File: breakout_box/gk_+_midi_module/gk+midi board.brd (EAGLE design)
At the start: 65.2 x 100 mm, 114 parts, among them Q1 QUARZ5, T1 2N2222, T2 2N2222, U1 LMV324, U3 L78LXX, U4 MIC5205-3.3, U5 MSP430G2553RHB32, U7 TLV2170DGKT

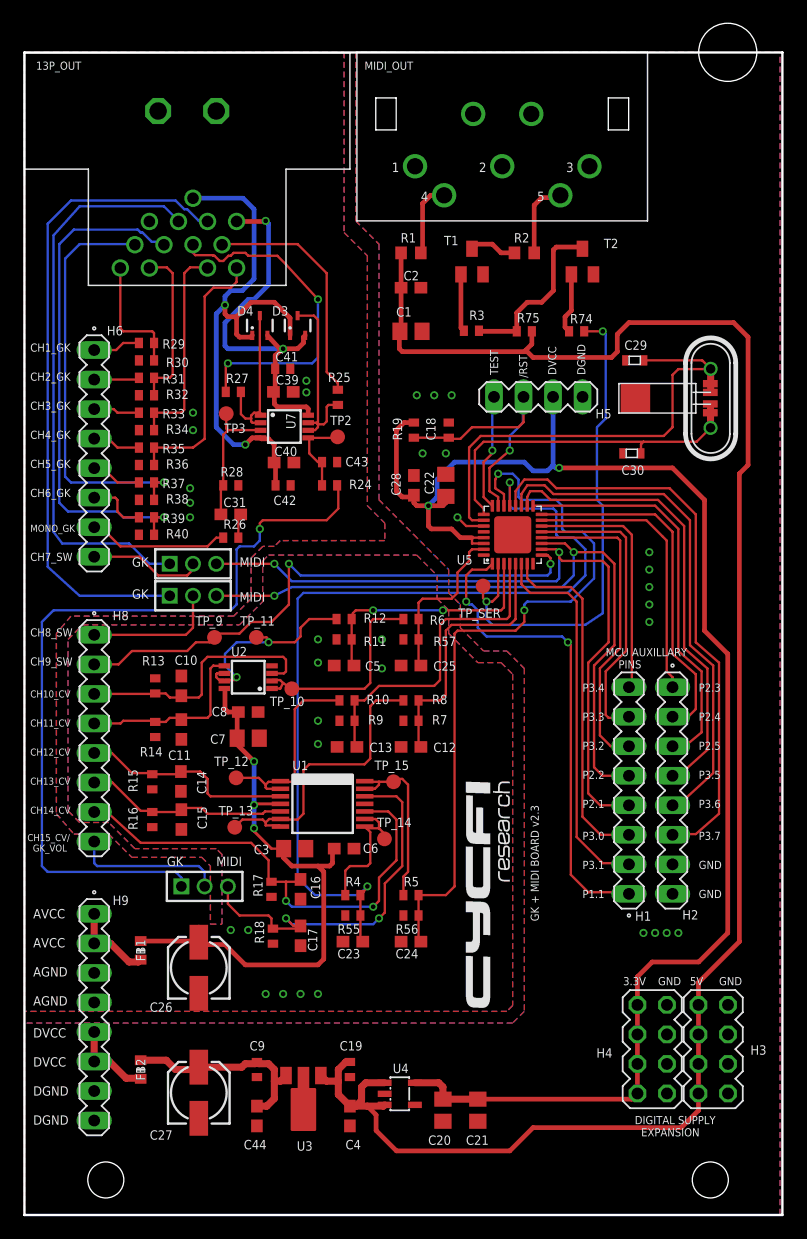
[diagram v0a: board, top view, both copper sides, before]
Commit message: update boms and pdf for shematics files
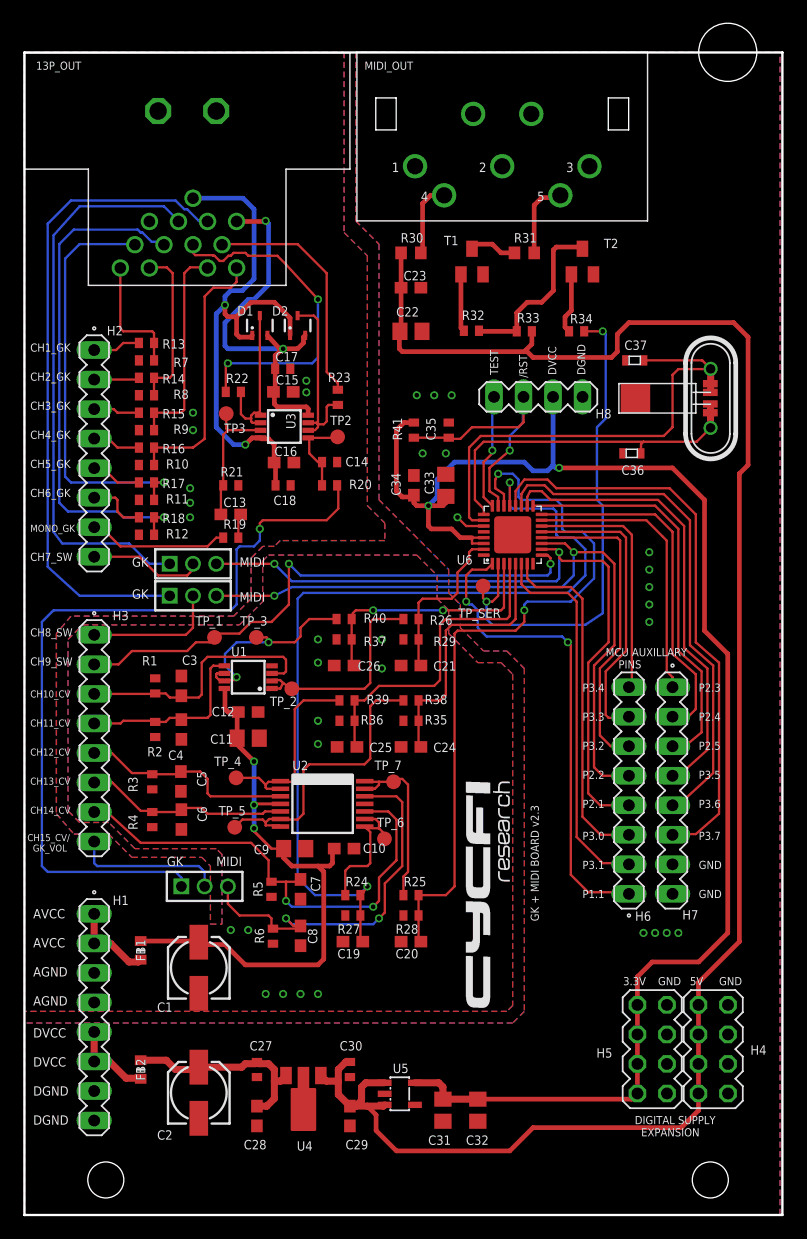
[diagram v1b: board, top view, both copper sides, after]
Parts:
- removed C39, C40: 4.7uF, resistor:C0603
- removed C41, C42: 0.1uF, resistor:C0402
- removed C43: 0.01uF, resistor:C0402
- removed C44: 0.1uF, resistor:C0603
- removed H9: (no value), con-lstb:MA08-1
- removed R55, R56, R57: 10k, resistor:R0402
- removed R74, R75: 1K, resistor:R0402
- removed U7: TLV2170DGKT, CYCFI_semicon:MSOP8
- added C32: 10uf, resistor:C0805
- added C33: 2.2uf, resistor:C0805
- added C34: 0.1uf, resistor:C0603
- added C35: 1nF, resistor:C0402
- added C36, C37: 12pF, ssmd:0603
- added H7: DNP, con-lstb:MA08-1
- added R20: 18K, resistor:R0402
- added R21: 470K, resistor:R0402
- added R22, R23: 100R, resistor:R0402
- added R41: 47K, resistor:R0402
- added U6: MSP430G2553RHB32, CYCFI_IC:QFN32
- C1: value 10uF -> 100uF; device resistor:C0805 -> resistor:153CLV-0505
- C11: value 0.1uF -> 10uF; device resistor:C0603 -> resistor:C0805
- C13: value 0.1uF -> 0.47uF
- C14: value 0.1uF -> 0.01uF; device resistor:C0603 -> resistor:C0402
- C15, C16: value 0.1uF -> 4.7uF
- C17: device resistor:C0603 -> resistor:C0402
- C18: value 1nF -> 0.1uF
- C19: value 1uF -> 0.1uF; device resistor:C0402 -> resistor:C0603
- C2: value 0.1uF -> 100uF; device resistor:C0603 -> resistor:153CLV-0505
- C20: value 33uf -> 0.1uF; device resistor:C0805 -> resistor:C0603
- C21: value 10uf -> 0.1uF; device resistor:C0805 -> resistor:C0603
- C22: value 2.2uf -> 10uF
- C26: value 100uF -> 0.1uF; device resistor:153CLV-0505 -> resistor:C0603
- C27: value 100uF -> 1uF; device resistor:153CLV-0505 -> resistor:C0402
- C28: value 0.1uf -> 0.1uF
- C29: value 12pF -> 0.1uF; device ssmd:0603 -> resistor:C0603
- C3, C7: value 10uF -> 0.1uF; device resistor:C0805 -> resistor:C0603
- C30: value 12pF -> 1uF; device ssmd:0603 -> resistor:C0402
- C31: value 0.47uF -> 33uf; device resistor:C0603 -> resistor:C0805
- C9: value 1uF -> 10uF; device resistor:C0402 -> resistor:C0805
- H1, H2: value DNP -> (none)
- H3: value DNP -> (none); device con-lstb:MA04-2 -> con-lstb:MA08-1
- H5: value (none) -> DNP; device con-lstb:MA04-1 -> con-lstb:MA04-2
- H6: value (none) -> DNP
- H8: device con-lstb:MA08-1 -> con-lstb:MA04-1
- R1, R2: value 220R -> 100K; device resistor:R0603 -> resistor:R0402
- R10, R12, R8: value 5.1k -> 5k
- R11, R7, R9: value 10k -> 5k
- R13, R14, R15, R16, R17, R18: value 100K -> 5k
- R19: value 47K -> 10K
- R24: value 18K -> 5.1k
- R25: value 100R -> 5.1k
- R26: value 10K -> 5.1k
- R27: value 100R -> 10k
- R28: value 470K -> 10k
- R29, R35, R36, R37: value 5k -> 10k
- R3: value 1K -> 100K
- R30, R31: value 5k -> 220R; device resistor:R0402 -> resistor:R0603
- R32, R33, R34: value 5k -> 1K
- R38, R39, R40: value 5k -> 5.1k
- R4, R5, R6: value 5.1k -> 100K
- U1: value LMV324 -> (none); device CYCFI_semicon:SSOP-14 -> CYCFI_semicon:MSOP8
- U2: value (none) -> LMV324; device CYCFI_semicon:MSOP8 -> CYCFI_semicon:SSOP-14
- U3: value L78LXX -> TLV2170DGKT; device CYCFI_Power:SOT89 -> CYCFI_semicon:MSOP8
- U4: value MIC5205-3.3 -> L78LXX; device v-reg-micrel:SOT23-5 -> CYCFI_Power:SOT89
- U5: value MSP430G2553RHB32 -> MIC5205-3.3; device CYCFI_IC:QFN32 -> v-reg-micrel:SOT23-5
- moved C2 71.6 mm to (15.0, 10.5), turned to 90 degrees
- moved C29 69.5 mm to (28.0, 8.50), turned to 270 degrees
- moved H3 59.6 mm to (6.00, 41.0), turned to 270 degrees
- moved C30 58.3 mm to (28.0, 12.5), turned to 270 degrees
- moved U3 57.8 mm to (22.4, 67.8), turned to 270 degrees
- moved C1 57.7 mm to (15.0, 21.2), turned to 90 degrees
- moved H2 57.6 mm to (6.00, 65.5)
- moved H5 57.0 mm to (54.0, 14.2), turned to 90 degrees
- moved C23 56.5 mm to (33.2, 79.8), turned to 0 degrees
- moved C28 55.9 mm to (20.0, 8.50), turned to 270 degrees
- moved C31 54.4 mm to (36.0, 9.00), turned to 270 degrees
- moved H6 54.4 mm to (52.0, 36.5), turned to 90 degrees
- moved R2 51.9 mm to (11.2, 41.8), turned to 90 degrees
- moved H1 50.0 mm to (6.00, 17.0), turned to 270 degrees
- moved U5 49.1 mm to (32.3, 10.4), turned to 270 degrees
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- renumbered D3 to D2, D4 to D1, TP_10 to TP_2, TP_11 to TP_3, TP_12 to TP_4, TP_13 to TP_5, TP_14 to TP_6, TP_15 to TP_7, TP_9 to TP_1, U$3 to U$1
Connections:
- net !RST: now also C35.1, H8.2, R41.2, U6.23; no longer C18.1, H5.2, R19.2, U5.23
- net +3.3V: now also C31.1, C32.1, C33.1, C34.1, H5.2, H5.4, H5.6, H5.8, H8.3, R41.1, U5.5, U6.29, U6.30; no longer C20.1, C21.1, C22.1, C28.1, H4.2, H4.4, H4.6, H4.8, H5.3, R19.1, U4.5, U5.29, U5.30
- net +5V: now also C22.1, C23.1, C29.1, C30.1, H4.2, H4.4, H4.6, H4.8, R30.1, R33.2, U5.1, U5.3; no longer C1.1, C19.1, C2.1, C4.1, H3.2, H3.4, H3.6, H3.8, R1.1, R75.2, U3.1, U4.3
- net +VE: now also C15.1, C17.1, U3.8; no longer C39.1, C41.1, U7.8
- net -VE: now also C16.2, C18.2, U3.4; no longer C40.2, C42.2, U7.4
- net AVCC: now also H1.1, H1.2; no longer H9.1, H9.2
- net CH10_CV: now also R26.1, U1.1, U1.2; no longer R6.1, U2.1, U2.2
- net CH11_CV: now also R40.2, U1.6, U1.7; no longer R12.2, U2.6, U2.7
- net CH12_CV: now also R39.2, U2.1, U2.2; no longer R10.2, U1.1, U1.2
- net CH13_CV: now also R38.2, U2.6, U2.7; no longer R8.2, U1.6, U1.7
- net CH14_CV: now also R24.1, U2.8, U2.9; no longer R4.1, U1.8, U1.9
- net CH15_CV: now also R25.1, U2.13, U2.14; no longer R5.1, U1.13, U1.14
- net CH15_CV_IN: now also C8.1, JP1.3, R6.2, U2.12; no longer C17.1, JP3.3, R18.2, U1.12
- net CH15_GK_VOL: now also JP1.1, R20.1; no longer JP3.1, R24.1
- net CH15_GK_VOL/CV: now also H3.8, JP1.2; no longer H8.8, JP3.2
- net CH1_GK: now also H2.1, R7.2; no longer H6.1, R30.2
- net CH2_GK: now also H2.2, R8.2; no longer H6.2, R32.2
- net CH3_GK: now also H2.3, R9.2; no longer H6.3, R34.2
- net CH4_GK: now also H2.4, R10.2; no longer H6.4, R36.2
- net CH5_GK: now also H2.5, R11.2; no longer H6.5, R38.2
- net CH6_GK: now also H2.6, R12.2; no longer H6.6, R40.2
- net CH7_CV_IN: now also H6.4, U6.10; no longer H1.4, U5.10
- net CH7_GK_SW/CV: now also H2.8; no longer H6.8
- net CH8_CV_IN: now also H6.5, JP3.3, U6.11; no longer H1.5, JP1.3, U5.11
- net CH8_GK_SW: now also JP3.1; no longer JP1.1
- net CH8_GK_SW/CV: now also H3.1, JP3.2; no longer H8.1, JP1.2
- net CH9_CV: now also H3.2, U6.9; no longer H8.2, U5.9
- net DVCC: now also H1.5, H1.6; no longer H9.5, H9.6
- net D_VIN: now also C2.+, C27.1, C28.1, U4.3; no longer C27.+, C44.1, C9.1, U3.3
- net GK_VOL: now also R23.2; no longer R25.2
- net GND: now also C1.-, C16.1, C18.1, C2.-, C26.2, C27.2, C29.2, C30.2, C31.2, C32.2, C33.2, C34.2, C35.2, C36.1, C37.1, H1.3, H1.4, H1.7, H1.8, H5.1, H5.3, H5.5, H5.7, H7.7, H7.8, H8.4, R1.1, R2.1, R21.2, R27.2, R29.2, R3.1, R35.2, R36.2, R37.2, R4.1, R5.1, R6.1, U1.4, U2.11, U4.2@1, U5.2, U6.27, U6.28; no longer C1.2, C13.2, C16.2, C18.2, C2.2, C26.-, C27.-, C29.1, C30.1, C39.2, C40.1, C41.2, C42.1, C43.2, C44.2, H2.7, H2.8, H3.1, H3.3, H3.5, H3.7, H5.4, H9.3, H9.4, H9.7, H9.8, R11.2, R29.1, R31.1, R33.1, R35.1, R37.1, R39.1, R55.2, R56.2, R57.2, R7.2, R9.2, U1.11, U2.4, U3.2, U3.2@1, U5.27, U5.28
- net MONO_GK: now also H2.7, R19.1; no longer H6.7, R26.1
- net N$1: now also R31.2; no longer R2.2
- net N$10: now also C3.1, H3.3, R1.2, U1.3; no longer C10.1, H8.3, R13.2, U2.3
- net N$11: now also C4.1, H3.4, R2.2, U1.5; no longer C11.1, H8.4, R14.2, U2.5
- net N$14: now also C5.1, H3.5, R3.2, U2.3; no longer C14.1, H8.5, R15.2, U1.3
- net N$19: now also C6.1, H3.6, R4.2, U2.5; no longer C15.1, H8.6, R16.2, U1.5
- net N$2: now also R31.1; no longer R2.1
- net N$20: now also C7.1, H3.7, R5.2, U2.10; no longer C16.1, H8.7, R17.2, U1.10
- net N$21: now also R22.1; no longer R27.1
- net N$3: now also R32.2; no longer R3.2
- net N$35: now also R23.1, U3.6, U3.7; no longer R25.1, U7.6, U7.7
- net N$36: now also C14.1, R20.2, U3.5; no longer C43.1, R24.2, U7.5
- net N$37: now also C13.2, R19.2; no longer C31.2, R26.2
- net N$38: now also C13.1, R21.1, U3.3; no longer C31.1, R28.1, U7.3
- net N$39: now also R22.2, U3.1, U3.2; no longer R27.2, U7.1, U7.2
- net N$42: now also R13.2, R7.1; no longer R29.2, R30.1
- net N$43: now also R14.2, R8.1; no longer R31.2, R32.1
- net N$44: now also R15.2, R9.1; no longer R33.2, R34.1
- net N$45: now also R10.1, R16.2; no longer R35.2, R36.1
- net N$46: now also R11.1, R17.2; no longer R37.2, R38.1
- net N$47: now also R12.1, R18.2; no longer R39.2, R40.1
- net N$5: now also R30.2; no longer R1.2
- net N$6: now also U6.32; no longer U5.32
- net N$8: now also R34.2; no longer R74.2
- net N$9: now also R32.1, R33.1; no longer R3.1, R75.1
- net NC: now also U6.8; no longer U5.8
- net P1.0: now also C21.1, R26.2, R29.1, U6.31; no longer C25.1, R57.1, R6.2, U5.31
- net P1.1: now also H6.1, U6.1; no longer H1.1, U5.1
- net P1.2: now also R34.1, U6.2; no longer R74.1, U5.2
- net P1.3: now also C26.1, R37.1, R40.1, U6.3; no longer C5.1, R11.1, R12.1, U5.3
- net P1.4: now also C25.1, R36.1, R39.1, U6.4; no longer C13.1, R10.1, R9.1, U5.4
- net P1.5: now also C24.1, R35.1, R38.1, U6.5; no longer C12.1, R7.1, R8.1, U5.5
- net P1.6: now also C19.1, R24.2, R27.1, U6.21; no longer C23.1, R4.2, R55.1, U5.21
- net P1.7: now also C20.1, R25.2, R28.1, U6.22; no longer C24.1, R5.2, R56.1, U5.22
- net P2.3: now also H7.1, U6.15; no longer H2.1, U5.15
- net P2.4: now also H7.2, U6.16; no longer H2.2, U5.16
- net P2.5: now also H7.3, U6.17; no longer H2.3, U5.17
- net P2.6: now also C37.2, U6.26; no longer C29.2, U5.26
- net P2.7: now also C36.2, U6.25; no longer C30.2, U5.25
- net P3.0: now also H6.3, U6.7; no longer H1.3, U5.7
- net P3.1: now also H6.2, U6.6; no longer H1.2, U5.6
- net P3.2: now also H6.6, U6.12; no longer H1.6, U5.12
- net P3.3: now also H6.7, U6.13; no longer H1.7, U5.13
- net P3.4: now also H6.8, U6.14; no longer H1.8, U5.14
- net P3.5: now also H7.4, U6.18; no longer H2.4, U5.18
- net P3.6: now also H7.5, U6.19; no longer H2.5, U5.19
- net P3.7: now also H7.6, U6.20; no longer H2.6, U5.20
- net TEST: now also H8.1, U6.24; no longer H5.1, U5.24
- net VIN: now also C1.+, C10.1, C11.1, C12.1, C9.1, U1.8, U2.4; no longer C26.+, C3.1, C6.1, C7.1, C8.1, U1.4, U2.8

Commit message: update shematic pdf
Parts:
- R10, R11, R12, R13, R14, R15, R16, R17, R18, R7, R8, R9: value 5k -> 5.1k
- renumbered Q1 to X1, U$1 to 13P-CN1
